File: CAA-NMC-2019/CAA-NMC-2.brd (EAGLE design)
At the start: 33.3 x 100 mm, 18 parts, among them IC1 ATTINY85-20SU, J1 M20-9980346

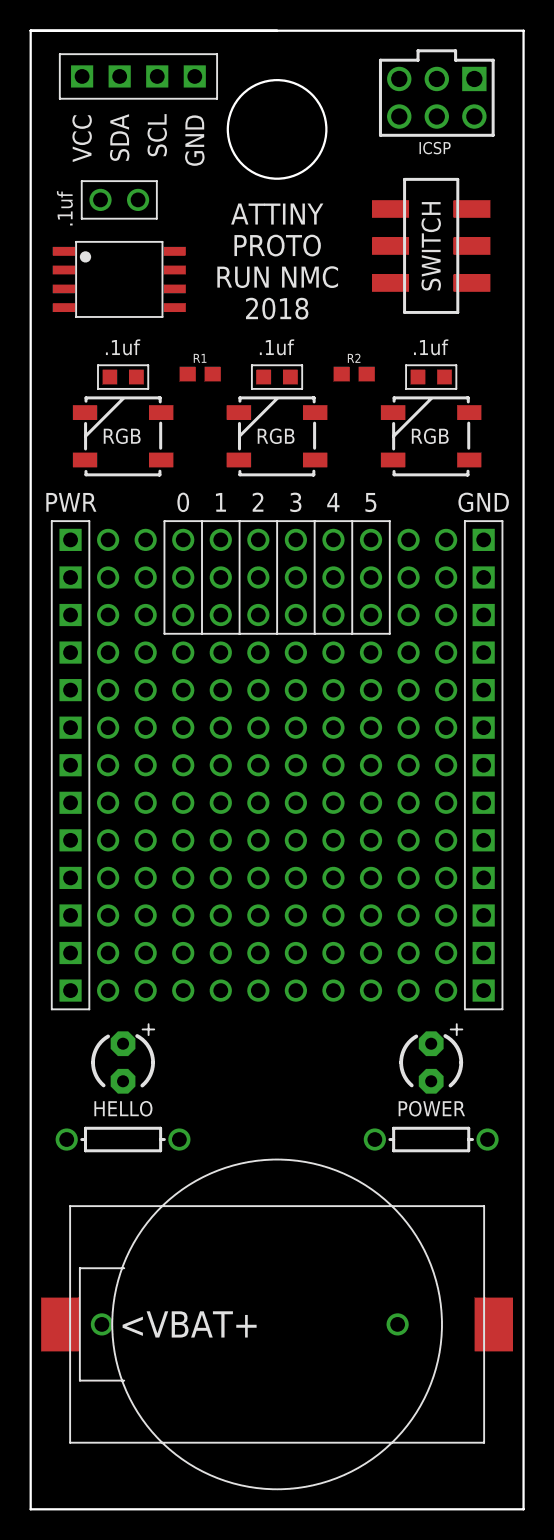
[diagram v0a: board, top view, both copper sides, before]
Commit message: nmc2 panelized for seeed
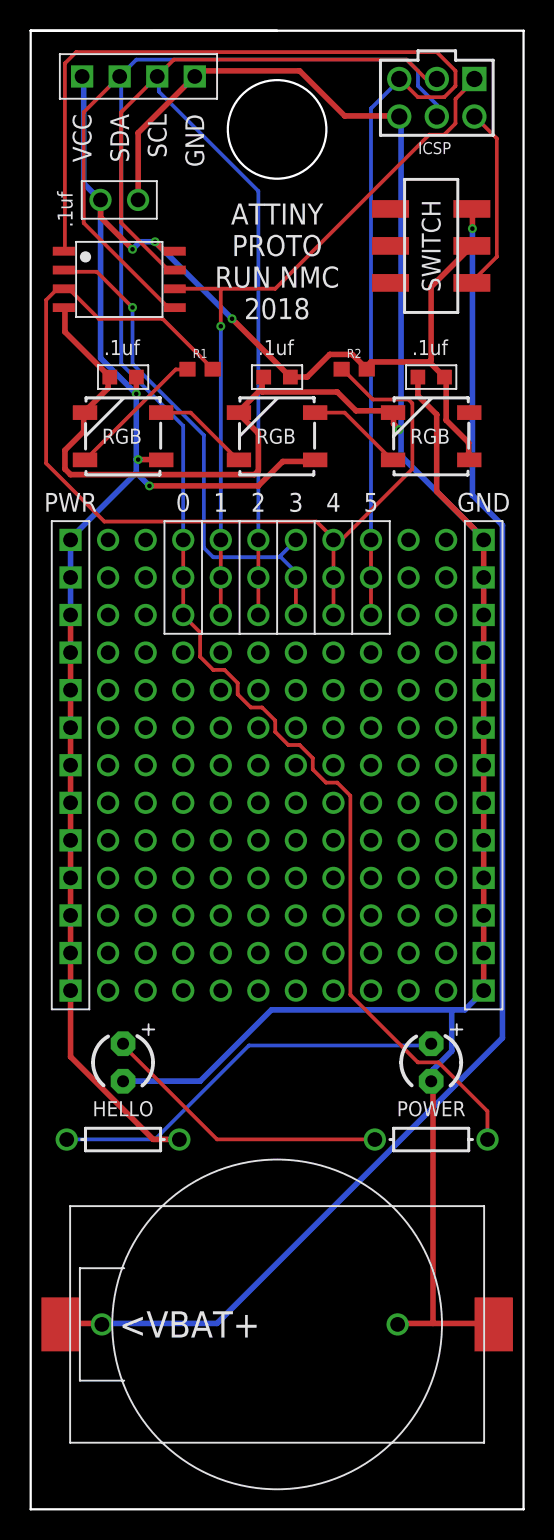
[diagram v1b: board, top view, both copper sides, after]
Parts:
- removed U$5: (no value), NickParts:OSHPARK_LOGOHEX
- moved R1 0.34 mm to (-5.21, 77.1)
- moved R2 0.34 mm to (5.21, 77.1)
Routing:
- net GND: track 0.00 -> 200.4 mm, vias 0 -> 1
- net VCC: track 0.00 -> 143.5 mm, vias 0 -> 6
- net PB0: track 0.00 -> 128.9 mm
- net VBAT: track 0.00 -> 94.9 mm, vias 0 -> 1
- net PB5: track 0.00 -> 82.7 mm
- net PB2: track 0.00 -> 75.1 mm
- net PB4: track 0.00 -> 69.1 mm
- net PB1: track 0.00 -> 49.2 mm, vias 0 -> 1
- net PB3: track 0.00 -> 35.4 mm, vias 0 -> 1
- net N$1: track 0.00 -> 27.4 mm
- net N$2: track 0.00 -> 19.8 mm
- net VUSB: track 0.00 -> 12.6 mm
- net N$5: track 0.00 -> 9.47 mm
- net N$4: track 0.00 -> 6.59 mm
- net N$3: track 0.00 -> 6.57 mm
